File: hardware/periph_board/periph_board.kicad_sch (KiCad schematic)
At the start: 45 parts, among them IC100 CD74HC4067SM96, IC101 LM2937ET-3.3_NOPB, IC102 MCP3221AxT-E_OT, J100 2x8 Socket Pins, J101 2x8 Plug Pins

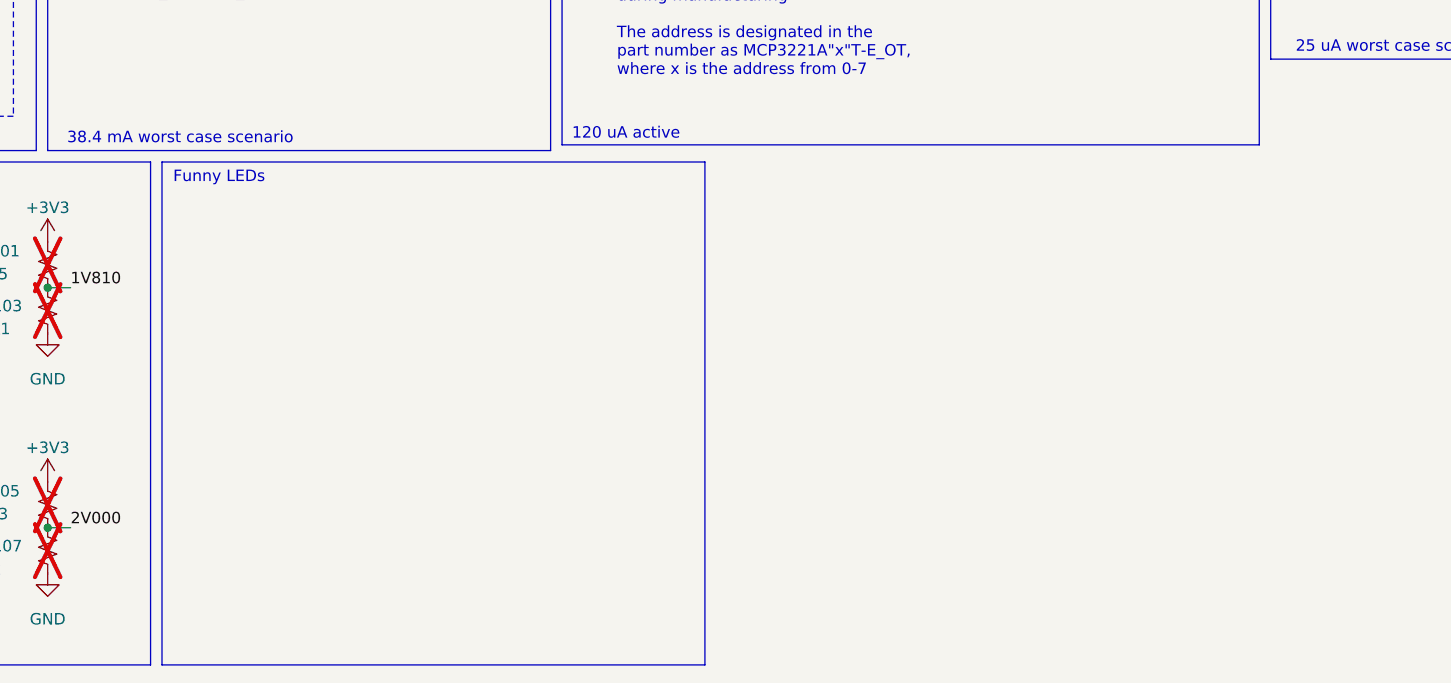
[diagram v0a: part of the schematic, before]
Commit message: added selection line LEDs to p board
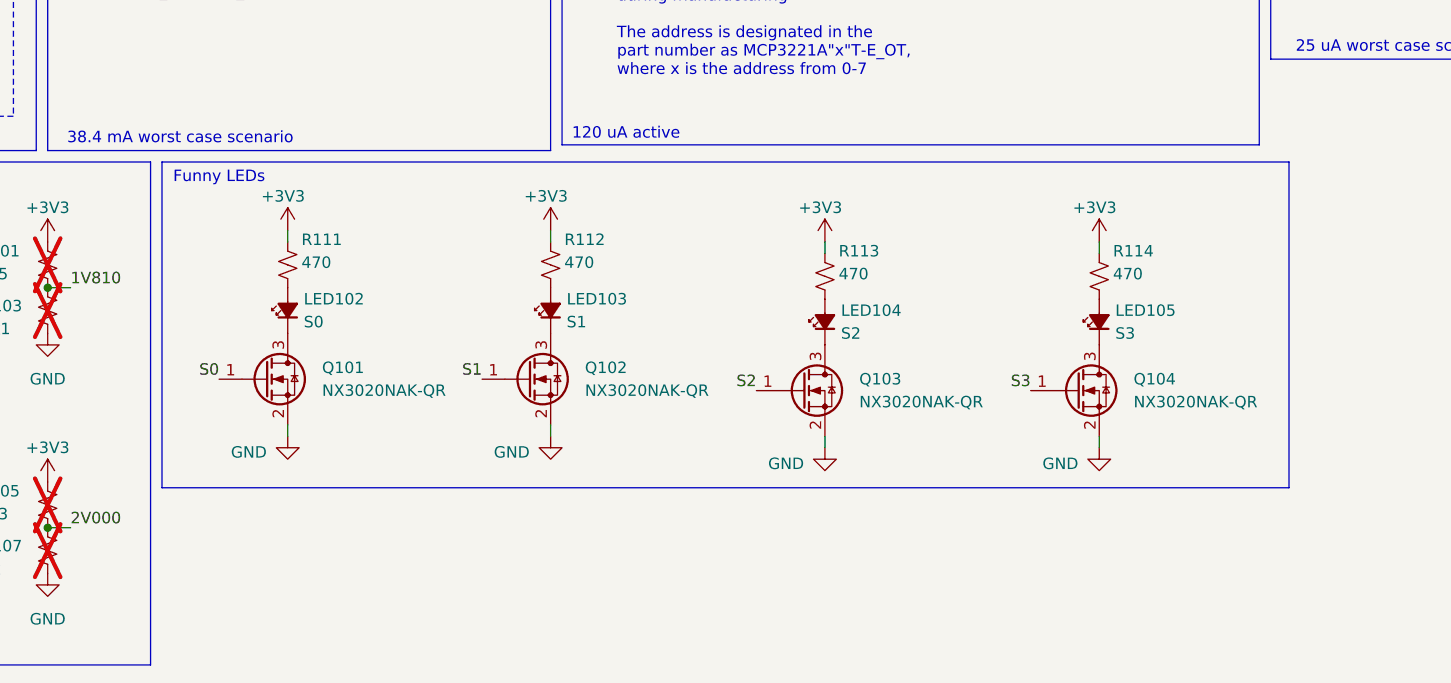
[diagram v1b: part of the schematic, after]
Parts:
- added LED102: S0, SamacSys_Parts:LEDC2012X40N, symbol Device:LED_Small_Filled
- added LED103: S1, SamacSys_Parts:LEDC2012X40N, symbol Device:LED_Small_Filled
- added LED104: S2, SamacSys_Parts:LEDC2012X40N, symbol Device:LED_Small_Filled
- added LED105: S3, SamacSys_Parts:LEDC2012X40N, symbol Device:LED_Small_Filled
- added Q101, Q102, Q103, Q104: NX3020NAK-QR, SamacSys_Parts:SOT95P230X110-3N, symbol Transistor_FET:Q_NMOS_GSD
- added R111, R112, R113, R114: 470, Resistor_SMD:R_0805_2012Metric, symbol Device:R_Small_US
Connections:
- net +3V3: now also R111.2, R112.2, R113.2, R114.2
- net GND: now also Q101.2 (S), Q102.2 (S), Q103.2 (S), Q104.2 (S)
- net S0: now also Q101.1 (G)
- net S1: now also Q102.1 (G)
- net S2: now also Q103.1 (G)
- net S3: now also Q104.1 (G)
- new net: LED102.1 (K), Q101.3 (D)
- new net: LED105.1 (K), Q104.3 (D)
- new net: LED105.2 (A), R114.1
- new net: LED102.2 (A), R111.1
- new net: LED104.2 (A), R113.1
- new net: LED103.1 (K), Q102.3 (D)
- new net: LED103.2 (A), R112.1
- new net: LED104.1 (K), Q103.3 (D)

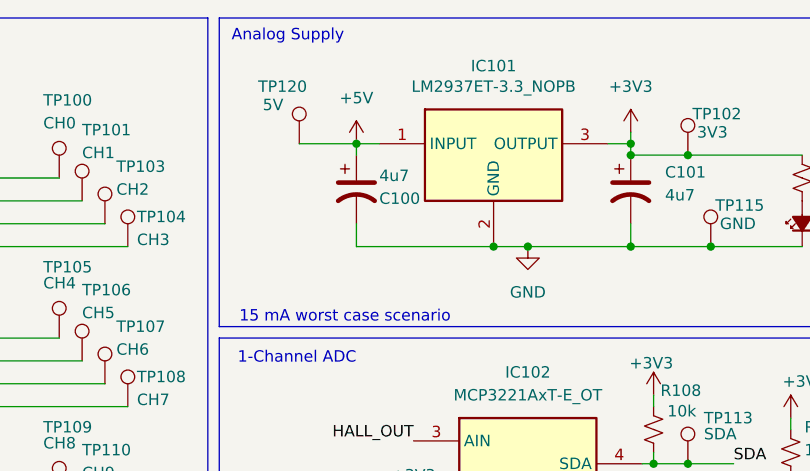
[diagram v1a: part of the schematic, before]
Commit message: changed level shifter. bunch of aesthetic changes. led resistors changed on main board. saving before nuke mouser.co.uk
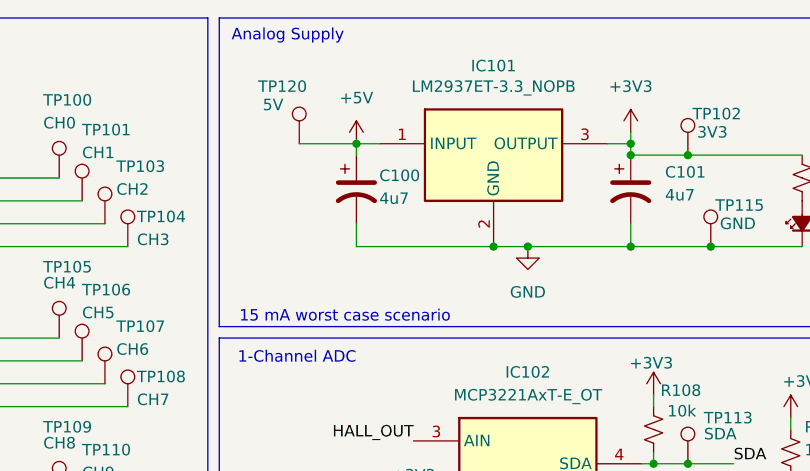
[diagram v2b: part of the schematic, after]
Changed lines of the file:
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@@
 		(dnp no)
 		(property "Reference" "C100"
-			(at 120.65 34.036 0)
+			(at 120.65 31.496 0)
 			(effects
 				(font
@@
 		)
 		(property "Value" "4u7"
-			(at 120.65 31.496 0)
+			(at 120.65 34.036 0)
 			(effects
 				(font

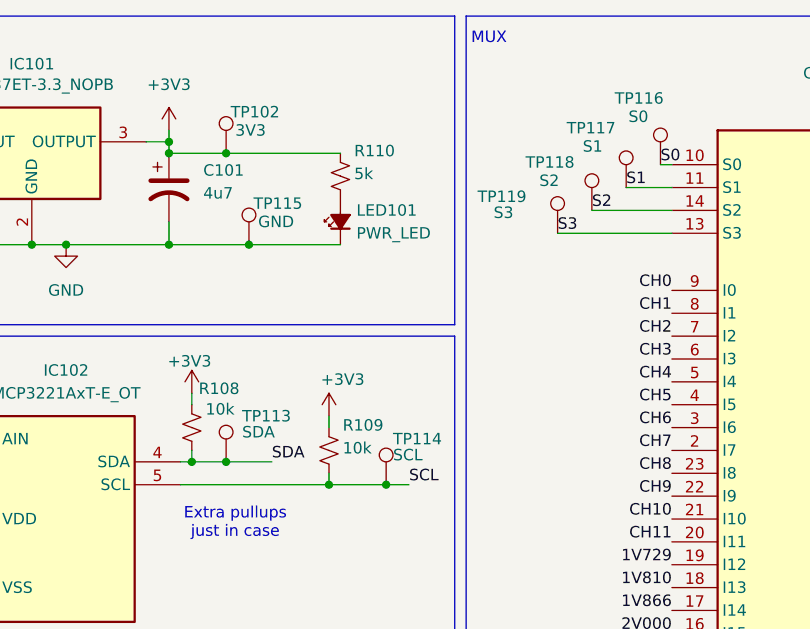
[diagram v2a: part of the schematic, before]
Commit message: finished everything except bom information. drc verification
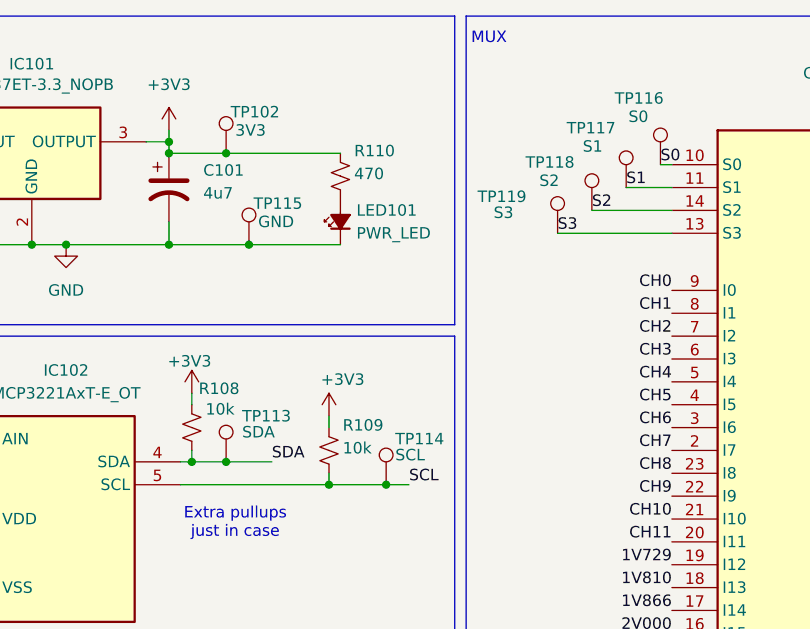
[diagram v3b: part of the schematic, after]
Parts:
- IC100: Mouser Price/Stock https://www.mouser.co.uk/ProductDetail/Texas-Instruments/CD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 -> https://www.mouser.com/ProductDetail/Texas-Instruments/CD74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
- IC101: Mouser Price/Stock https://www.mouser.co.uk/ProductDetail/Texas-Instruments/LM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 -> https://www.mouser.com/ProductDetail/Texas-Instruments/LM29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
- IC102: Mouser Price/Stock https://www.mouser.co.uk/ProductDetail/Microchip-Technology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 -> https://www.mouser.com/ProductDetail/Microchip-Technology/M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
- LED101, LED102, LED103, LED104, LED105: Mouser Price/Stock https://www.mouser.co.uk/ProductDetail/ams-OSRAM/LS-R976-NR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 -> https://www.mouser.com/ProductDetail/ams-OSRAM/LS-R976-NR-1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
- R100, R101, R102, R103, R104, R105, R106, R107: footprint Resistor_SMD:R_0805_2012Metric_Pad1.20x1.40mm_HandSolder -> Resistor_SMD:R_0805_2012Metric
- R110: value 5k -> 470
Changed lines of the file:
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@@
 			)
 		)
-		(property "Footprint" "Resistor_SMD:R_0805_2012Metric_Pad1.20x1.40mm_HandSolder"
+		(property "Footprint" "Resistor_SMD:R_0805_2012Metric"
 			(at 45.72 151.13 0)
 			(effects
@@
 			)
 		)
-		(property "Mouser Price/Stock" "https://www.mouser.co.uk/ProductDetail/Microchip-Technology/MCP3221A5T-E-OT?qs=InakTnyiSK9lljladcdZHQ%3D%3D"
+		(property "Mouser Price/Stock" "https://www.mouser.com/ProductDetail/Microchip-Technology/MCP3221A5T-E-OT?qs=InakTnyiSK9lljladcdZHQ%3D%3D"
 			(at 146.05 655.88 0)
 			(effects
@@
 			)
 		)
-		(property "Mouser Price/Stock" "https://www.mouser.co.uk/ProductDetail/Texas-Instruments/LM2937ET-3.3-NOPB?qs=X1J7HmVL2ZEMUke2IfNR4w%3D%3D"
+		(property "Mouser Price/Stock" "https://www.mouser.com/ProductDetail/Texas-Instruments/LM2937ET-3.3-NOPB?qs=X1J7HmVL2ZEMUke2IfNR4w%3D%3D"
 			(at 142.24 621.59 0)
 			(effects
@@
 			)
 		)
-		(property "Mouser Price/Stock" "https://www.mouser.co.uk/ProductDetail/Texas-Instruments/CD74HC4067SM96?qs=JHHQeKcAU3DyfvAOSRLjhQ%3D%3D"
+		(property "Mouser Price/Stock" "https://www.mouser.com/ProductDetail/Texas-Instruments/CD74HC4067SM96?qs=JHHQeKcAU3DyfvAOSRLjhQ%3D%3D"
 			(at 246.38 620.32 0)
 			(effects
@@
 		(dnp no)
 		(property "Reference" "TP114"
-			(at 173.482 60.96 0)
+			(at 173.736 60.96 0)
 			(effects
 				(font
@@
 		)
 		(property "Value" "SCL"
-			(at 173.482 62.738 0)
+			(at 173.736 62.738 0)
 			(effects
 				(font
@@
 			)
 		)
-		(property "Footprint" "Resistor_SMD:R_0805_2012Metric_Pad1.20x1.40mm_HandSolder"
+		(property "Footprint" "Resistor_SMD:R_0805_2012Metric"
 			(at 26.67 119.38 0)
 			(effects
@@
 			)
 		)
-		(property "Footprint" "Resistor_SMD:R_0805_2012Metric_Pad1.20x1.40mm_HandSolder"
+		(property "Footprint" "Resistor_SMD:R_0805_2012Metric"
 			(at 26.67 124.46 0)
 			(effects
@@
 			)
 		)
-		(property "Mouser Price/Stock" "https://www.mouser.co.uk/ProductDetail/ams-OSRAM/LS-R976-NR-1?qs=K5ta8V%252BWhtZhvCAe1sTZFg%3D%3D"
+		(property "Mouser Price/Stock" "https://www.mouser.com/ProductDetail/ams-OSRAM/LS-R976-NR-1?qs=K5ta8V%252BWhtZhvCAe1sTZFg%3D%3D"
 			(at 756.21 113.03 0)
 			(effects
@@
 			)
 		)
-		(property "Footprint" "Resistor_SMD:R_0805_2012Metric_Pad1.20x1.40mm_HandSolder"
+		(property "Footprint" "Resistor_SMD:R_0805_2012Metric"
 			(at 45.72 124.46 0)
 			(effects
@@
 			)
 		)
-		(property "Mouser Price/Stock" "https://www.mouser.co.uk/ProductDetail/ams-OSRAM/LS-R976-NR-1?qs=K5ta8V%252BWhtZhvCAe1sTZFg%3D%3D"
+		(property "Mouser Price/Stock" "https://www.mouser.com/ProductDetail/ams-OSRAM/LS-R976-NR-1?qs=K5ta8V%252BWhtZhvCAe1sTZFg%3D%3D"
 			(at 761.29 24.13 0)
 			(effects
@@
 			)
 		)
-		(property "Footprint" "Resistor_SMD:R_0805_2012Metric_Pad1.20x1.40mm_HandSolder"
+		(property "Footprint" "Resistor_SMD:R_0805_2012Metric"
 			(at 45.72 119.38 0)
 			(effects
@@
 			)
 		)
-		(property "Mouser Price/Stock" "https://www.mouser.co.uk/ProductDetail/ams-OSRAM/LS-R976-NR-1?qs=K5ta8V%252BWhtZhvCAe1sTZFg%3D%3D"
+		(property "Mouser Price/Stock" "https://www.mouser.com/ProductDetail/ams-OSRAM/LS-R976-NR-1?qs=K5ta8V%252BWhtZhvCAe1sTZFg%3D%3D"
 			(at 695.25 111.76 0)
 			(effects
@@
 			)
 		)
-		(property "Footprint" "Resistor_SMD:R_0805_2012Metric_Pad1.20x1.40mm_HandSolder"
+		(property "Footprint" "Resistor_SMD:R_0805_2012Metric"
 			(at 26.67 146.05 0)
 			(effects
@@
 			)
 		)
-		(property "Mouser Price/Stock" "https://www.mouser.co.uk/ProductDetail/ams-OSRAM/LS-R976-NR-1?qs=K5ta8V%252BWhtZhvCAe1sTZFg%3D%3D"
+		(property "Mouser Price/Stock" "https://www.mouser.com/ProductDetail/ams-OSRAM/LS-R976-NR-1?qs=K5ta8V%252BWhtZhvCAe1sTZFg%3D%3D"
 			(at 725.73 113.03 0)
 			(effects
@@
 			)
 		)
-		(property "Footprint" "Resistor_SMD:R_0805_2012Metric_Pad1.20x1.40mm_HandSolder"
+		(property "Footprint" "Resistor_SMD:R_0805_2012Metric"
 			(at 26.67 151.13 0)
 			(effects
@@
 			)
 		)
-		(property "Mouser Price/Stock" "https://www.mouser.co.uk/ProductDetail/ams-OSRAM/LS-R976-NR-1?qs=K5ta8V%252BWhtZhvCAe1sTZFg%3D%3D"
+		(property "Mouser Price/Stock" "https://www.mouser.com/ProductDetail/ams-OSRAM/LS-R976-NR-1?qs=K5ta8V%252BWhtZhvCAe1sTZFg%3D%3D"
 			(at 666.04 111.76 0)
 			(effects
@@
 			)
 		)
-		(property "Value" "5k"
+		(property "Value" "470"
 			(at 169.164 31.496 0)
 			(effects
@@
 			)
 		)
-		(property "Footprint" "Resistor_SMD:R_0805_2012Metric_Pad1.20x1.40mm_HandSolder"
+		(property "Footprint" "Resistor_SMD:R_0805_2012Metric"
 			(at 45.72 146.05 0)
 			(effects

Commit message: led info
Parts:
- LED102, LED103, LED104, LED105: Mouser Price/Stock https://www.mouser.com/ProductDetail/ams-OSRAM/LS-R976-NR-1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 -> (none)
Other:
- note added: "GRN"
- note added: "RED"
- moved on the sheet: LED104, LED105, Q103, Q104, R113, R114
